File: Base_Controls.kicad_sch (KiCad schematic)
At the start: 8 parts, among them J1 Mult_A, J2 JackA1, J3 JackA2, J4 JackA3, J5 JackA4, J6 JackA5, J7 Eurorack_10_pin_power

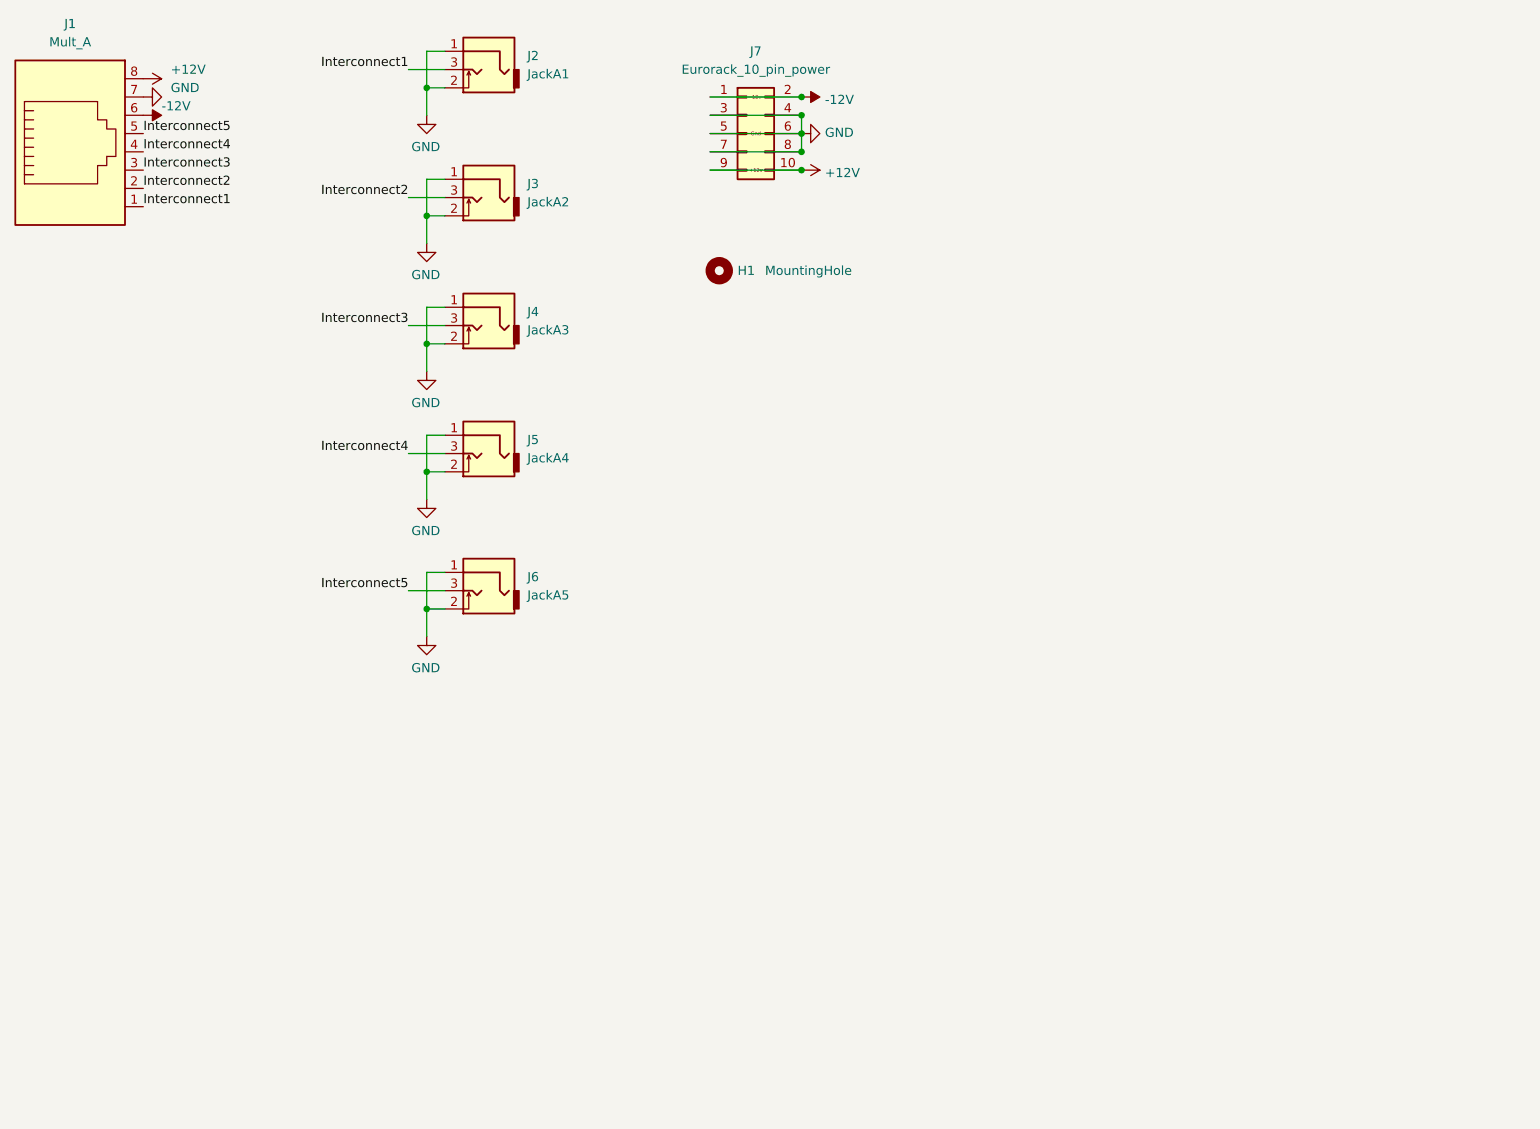
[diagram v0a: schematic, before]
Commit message: Fixed normal to ground of base unit jacks
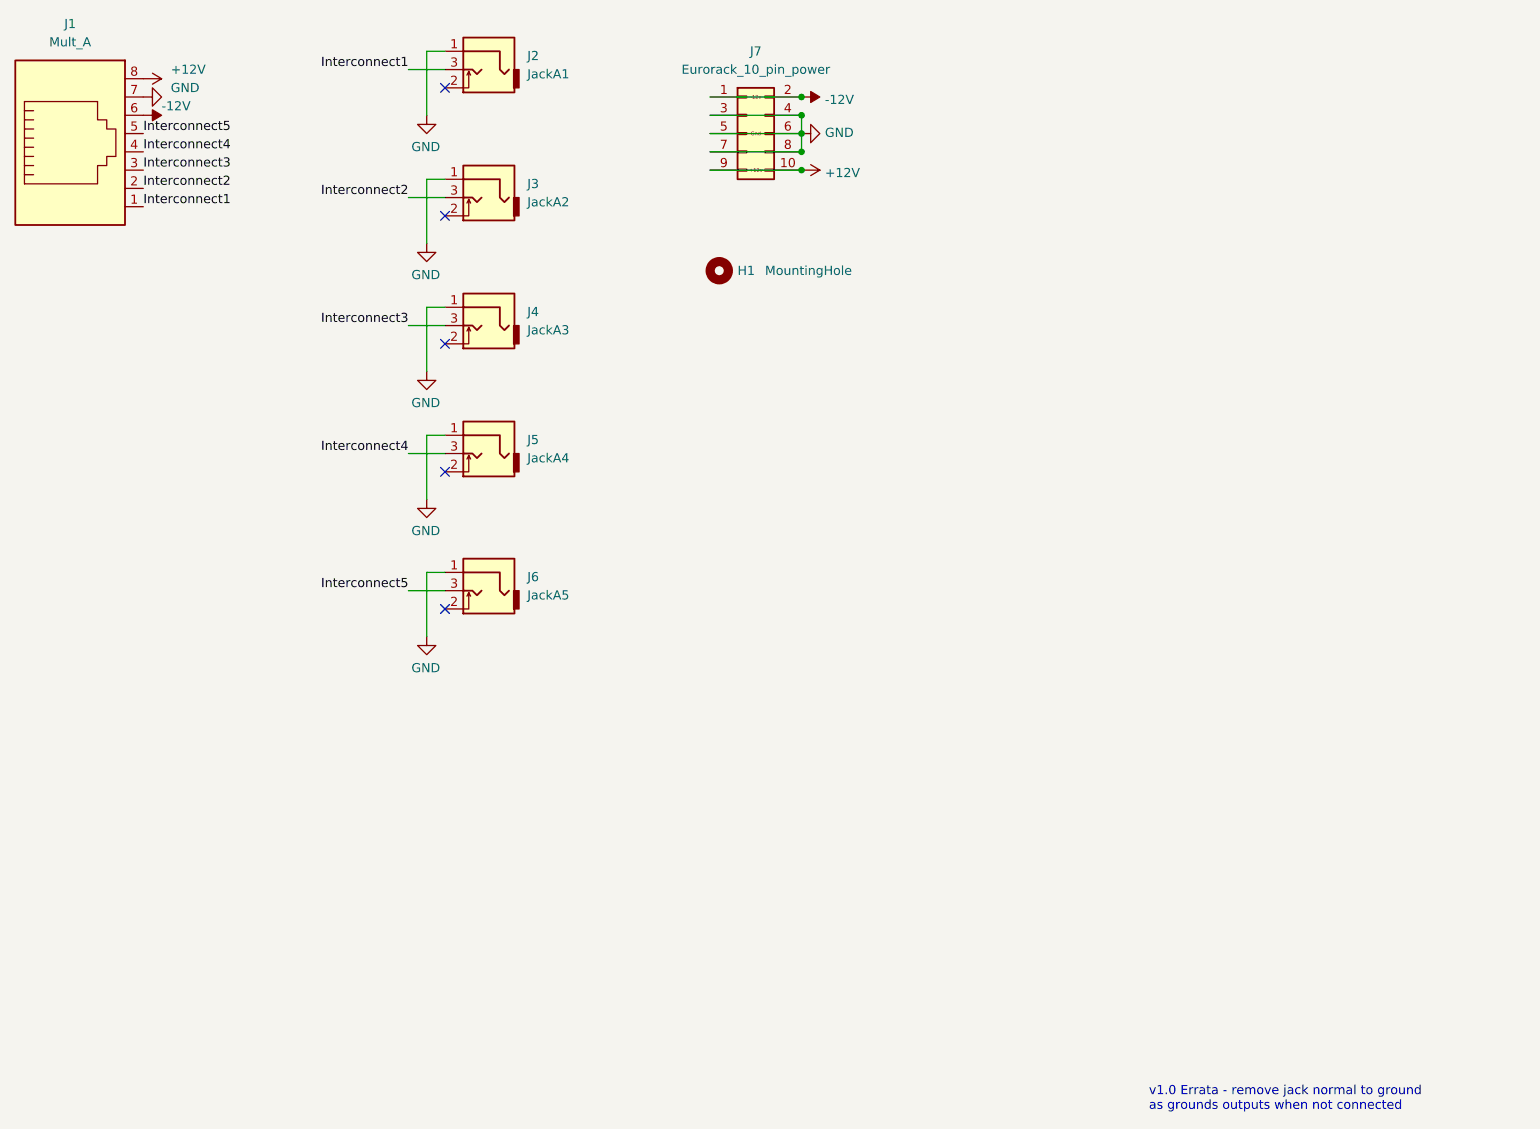
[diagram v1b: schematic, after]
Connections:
- net GND: no longer J2.2, J3.2, J4.2, J5.2, J6.2
- no-connect marks 0 -> 5
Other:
- note added: "v1.0 Errata - remove jack normal to ground as grounds outputs when not connected"
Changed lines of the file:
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@@
   (junction (at 132.08 31.75) (diameter 0) (color 0 0 0 0)
-  )
-  (junction (at 80.01 48.26) (diameter 0) (color 0 0 0 0)
-  )
-  (junction (at 80.01 30.48) (diameter 0) (color 0 0 0 0)
   )
   (junction (at 132.08 41.91) (diameter 0) (color 0 0 0 0)
@@
   (junction (at 132.08 36.83) (diameter 0) (color 0 0 0 0)
   )
-  (junction (at 80.01 66.04) (diameter 0) (color 0 0 0 0)
-  )
   (junction (at 132.08 39.37) (diameter 0) (color 0 0 0 0)
-  )
-  (junction (at 80.01 83.82) (diameter 0) (color 0 0 0 0)
   )
   (junction (at 132.08 34.29) (diameter 0) (color 0 0 0 0)
   )
-  (junction (at 80.01 102.87) (diameter 0) (color 0 0 0 0)
-  )
-  (wire (pts (xy 80.01 66.04) (xy 82.55 66.04))
-    (stroke (width 0) (type default))
-  )
+  (no_connect (at 82.55 102.87))
+  (no_connect (at 82.55 30.48))
+  (no_connect (at 82.55 48.26))
+  (no_connect (at 82.55 66.04))
+  (no_connect (at 82.55 83.82))
   (wire (pts (xy 119.38 34.29) (xy 132.08 34.29))
     (stroke (width 0) (type default))
   )
-  (wire (pts (xy 80.01 48.26) (xy 80.01 52.07))
+  (wire (pts (xy 80.01 43.18) (xy 80.01 52.07))
     (stroke (width 0) (type default))
   )
@@
     (stroke (width 0) (type default))
   )
-  (wire (pts (xy 80.01 66.04) (xy 80.01 69.85))
+  (wire (pts (xy 80.01 60.96) (xy 80.01 69.85))
     (stroke (width 0) (type default))
   )
-  (wire (pts (xy 80.01 78.74) (xy 80.01 83.82))
+  (wire (pts (xy 80.01 78.74) (xy 80.01 87.63))
     (stroke (width 0) (type default))
   )
@@
     (stroke (width 0) (type default))
   )
-  (wire (pts (xy 80.01 102.87) (xy 82.55 102.87))
-    (stroke (width 0) (type default))
-  )
-  (wire (pts (xy 80.01 30.48) (xy 82.55 30.48))
-    (stroke (width 0) (type default))
-  )
   (wire (pts (xy 82.55 43.18) (xy 80.01 43.18))
     (stroke (width 0) (type default))
@@
     (stroke (width 0) (type default))
   )
-  (wire (pts (xy 80.01 30.48) (xy 80.01 34.29))
+  (wire (pts (xy 80.01 25.4) (xy 80.01 34.29))
     (stroke (width 0) (type default))
   )
@@
     (stroke (width 0) (type default))
   )
-  (wire (pts (xy 80.01 43.18) (xy 80.01 48.26))
-    (stroke (width 0) (type default))
-  )
   (wire (pts (xy 119.38 39.37) (xy 132.08 39.37))
     (stroke (width 0) (type default))
@@
     (stroke (width 0) (type default))
   )
-  (wire (pts (xy 80.01 97.79) (xy 80.01 102.87))
-    (stroke (width 0) (type default))
-  )
-  (wire (pts (xy 80.01 48.26) (xy 82.55 48.26))
-    (stroke (width 0) (type default))
-  )
-  (wire (pts (xy 80.01 25.4) (xy 80.01 30.48))
+  (wire (pts (xy 80.01 97.79) (xy 80.01 106.68))
     (stroke (width 0) (type default))
   )
   (wire (pts (xy 82.55 81.28) (xy 77.47 81.28))
-    (stroke (width 0) (type default))
-  )
-  (wire (pts (xy 80.01 83.82) (xy 82.55 83.82))
-    (stroke (width 0) (type default))
-  )
-  (wire (pts (xy 80.01 60.96) (xy 80.01 66.04))
-    (stroke (width 0) (type default))
-  )
-  (wire (pts (xy 80.01 102.87) (xy 80.01 106.68))
     (stroke (width 0) (type default))
   )
@@
     (stroke (width 0) (type default))
   )
-  (wire (pts (xy 80.01 83.82) (xy 80.01 87.63))
-    (stroke (width 0) (type default))
-  )
   (wire (pts (xy 119.38 36.83) (xy 132.08 36.83))
     (stroke (width 0) (type default))
   )
+  (text "v1.0 Errata - remove jack normal to ground \nas grounds outputs when not connected"
+    (at 180.34 172.72 0)
+    (effects (font (size 1.27 1.27)) (justify left bottom))
+  )
   (label "Interconnect5" (at 77.47 100.33 180) (fields_autoplaced)
